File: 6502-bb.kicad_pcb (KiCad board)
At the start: 2 copper layers, 128.9 x 81.3 mm, 53 parts, among them J4 Conn_01x16, J5 Conn_01x08, J7 Conn_01x08

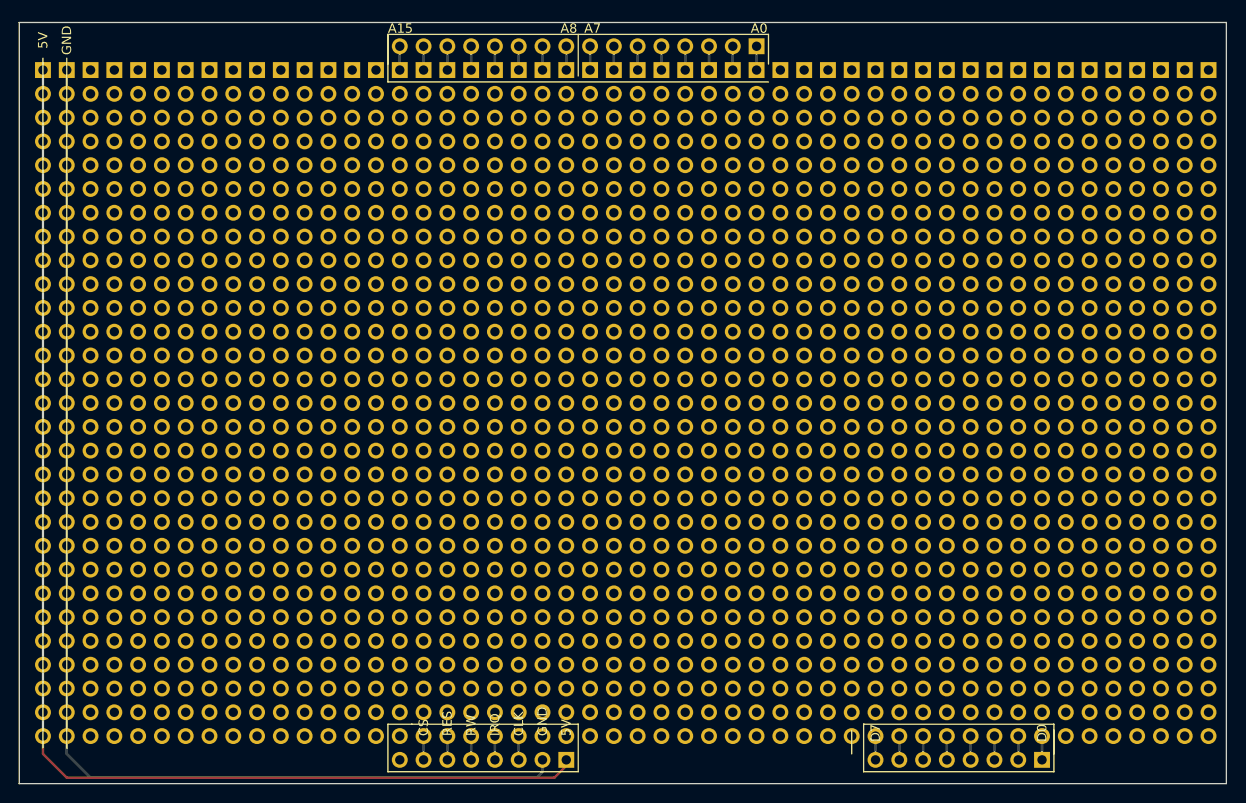
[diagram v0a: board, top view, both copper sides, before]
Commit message: Removed pinheaders from 3D view
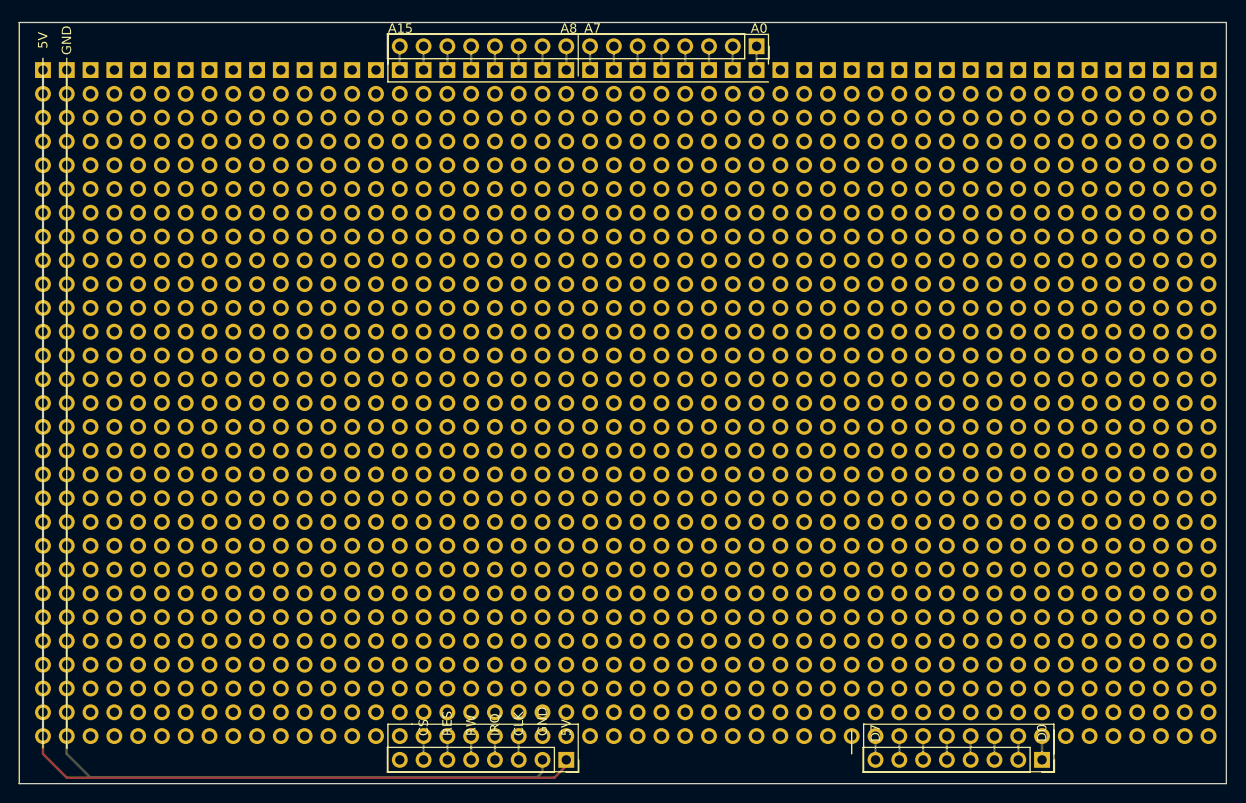
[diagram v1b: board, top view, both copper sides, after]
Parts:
- J4: footprint Connector_PinHeader_2.54mm:PinHeader_1x16_P2.54mm_Vertical -> Connector_PinSocket_2.54mm:PinSocket_1x16_P2.54mm_Vertical; moved to F.Cu
- J5, J7: footprint Connector_PinHeader_2.54mm:PinHeader_1x08_P2.54mm_Vertical -> Connector_PinSocket_2.54mm:PinSocket_1x08_P2.54mm_Vertical; moved to F.Cu
- turned J4 to 270 degrees
- turned J5 to 270 degrees
- turned J7 to 270 degrees
